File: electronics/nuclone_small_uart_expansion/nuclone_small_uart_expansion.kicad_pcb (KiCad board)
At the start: 2 copper layers, 50 x 50 mm, 87 parts, among them J1 USB-C_PD_USB, J2 Conn_01x16, J3 nuclone_small_left, J4 nuclone_small_right, J5 127, J6 127, J7 127, J8 127, U1 TPESD0504C6, U2 CH340B

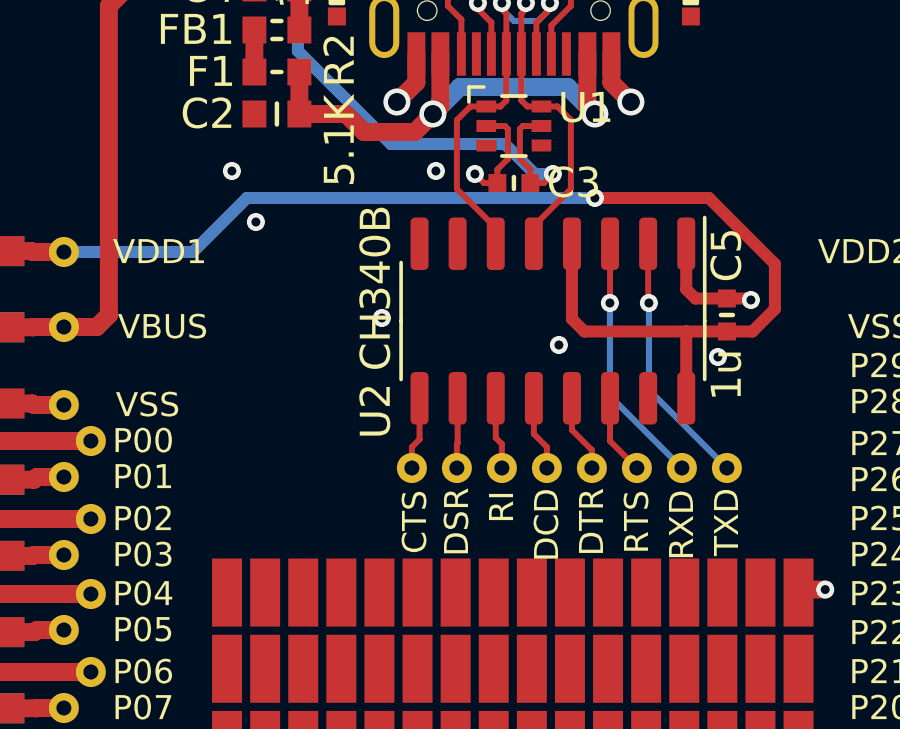
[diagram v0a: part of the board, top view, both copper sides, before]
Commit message: updated versionnumber, added activity led
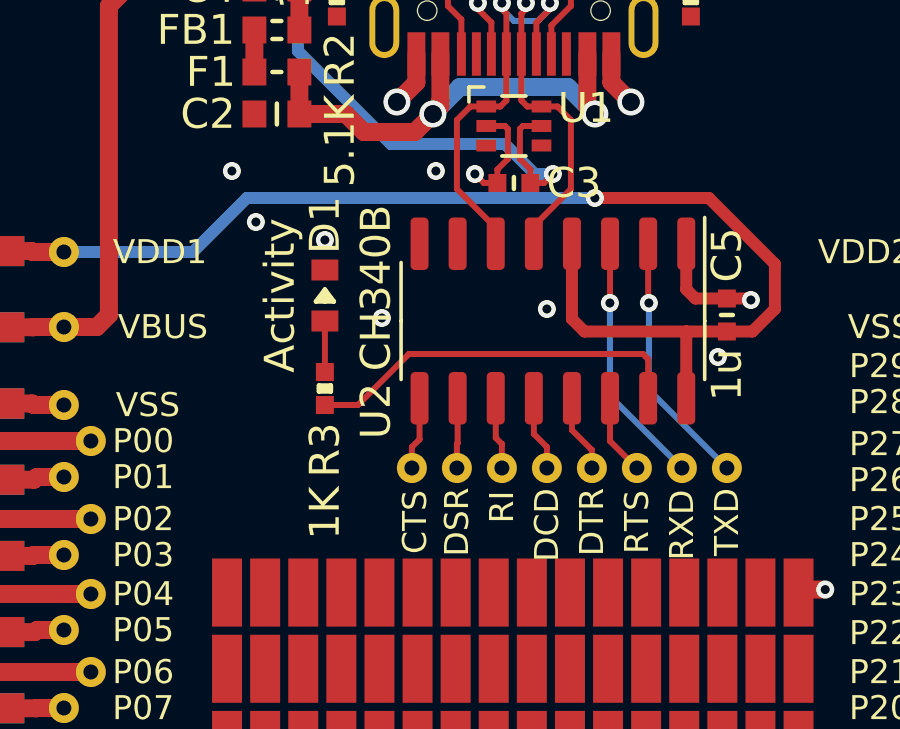
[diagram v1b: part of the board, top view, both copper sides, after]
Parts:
- added D1: Activity, SquantorDiodes:LED_0603_hand, F.Cu at (78.7, 76.0)
- added R3: 1K, SquantorRcl:R_0402_hand, F.Cu at (78.7, 79.2)
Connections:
- U2 pad 15: Net-(U2-Pad15) -> /TNOW
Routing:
- net /TNOW: track 0.00 -> 12.9 mm
- net Net-(D1-Pad2): track 0.00 -> 1.70 mm
- net /VSS: vias 26 -> 27

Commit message: updated versionnumber
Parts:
- N2: value V20220215 -> V20220306
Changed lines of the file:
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@@
       (effects (font (size 1 1) (thickness 0.15)) (justify mirror))
     )
-    (fp_text value V20220215 (at 0 0.1) (layer B.SilkS)
+    (fp_text value V20220306 (at 0 0.1) (layer B.SilkS)
       (effects (font (size 0.8 0.8) (thickness 0.15)) (justify mirror))
     )
